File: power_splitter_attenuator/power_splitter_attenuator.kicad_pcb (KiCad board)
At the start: 4 copper layers, 46.2 x 46.2 mm, 40 parts, among them J1 SMA, J2 SMA, J3 SMA, J4 SMA, J5 SMA, J6 SMA, J7 SMA, J8 SMA

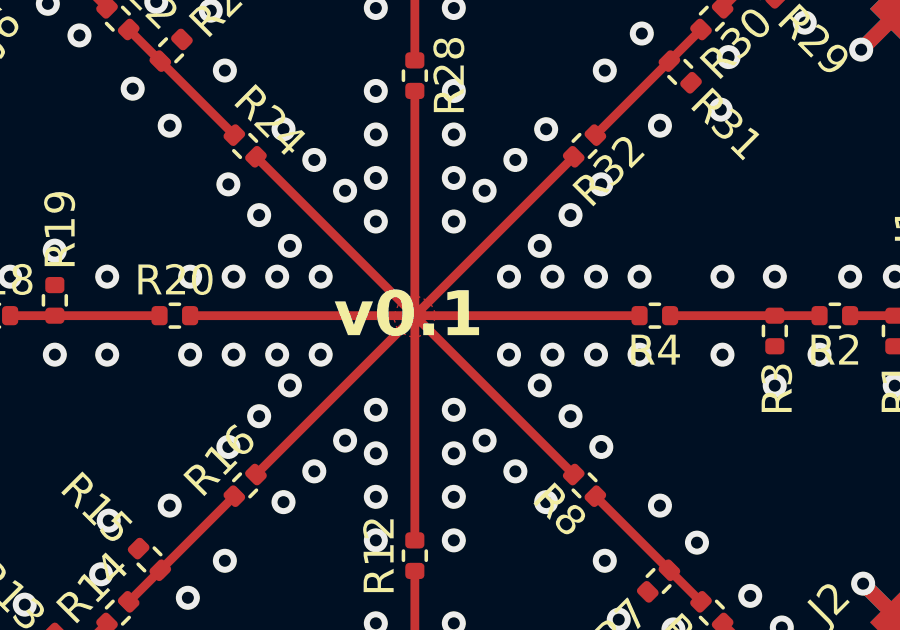
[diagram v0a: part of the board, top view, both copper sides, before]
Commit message: power splitter: update version number to 0.1.1
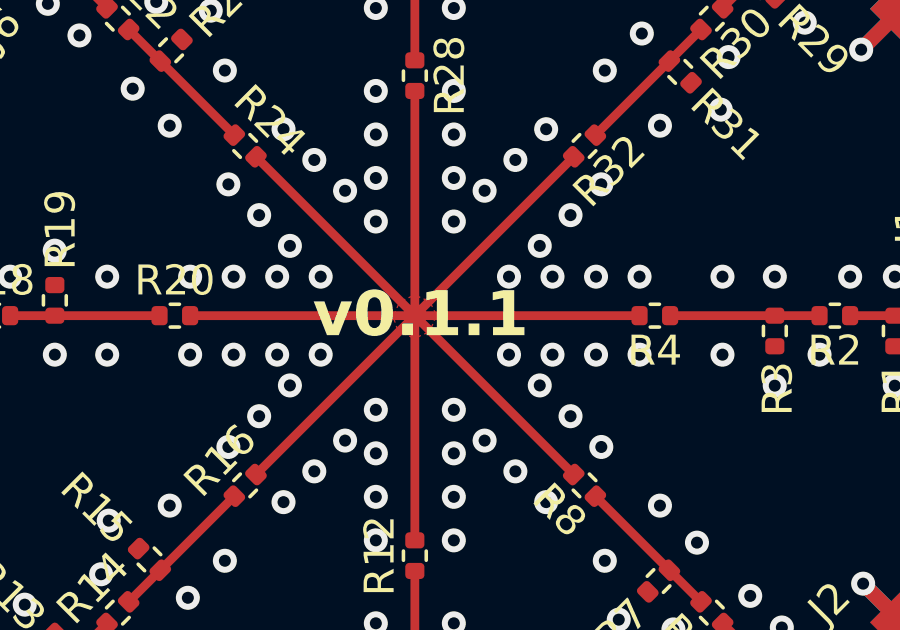
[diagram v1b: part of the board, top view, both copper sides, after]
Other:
- board text added: "v0.1.1"
- board text removed: "v0.1"
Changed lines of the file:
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@@
       (drillshape 0)
       (scaleselection 1)
-      (outputdirectory "output/v0.1.0/gerber/")
+      (outputdirectory "output/v0.1.1/gerber/")
     )
   )
@@
   (gr_circle (center 151.122048 100.092436) (end 152.422048 100.092436)
     (stroke (width 0.1) (type default)) (fill none) (layer "Edge.Cuts"))
-  (gr_text "v0.1" (at 140 80.6) (layer "F.SilkS")
+  (gr_text "v0.1.1" (at 139.3 80.6) (layer "F.SilkS")
     (effects (font (size 1.5 1.5) (thickness 0.3) bold) (justify left bottom))
   )

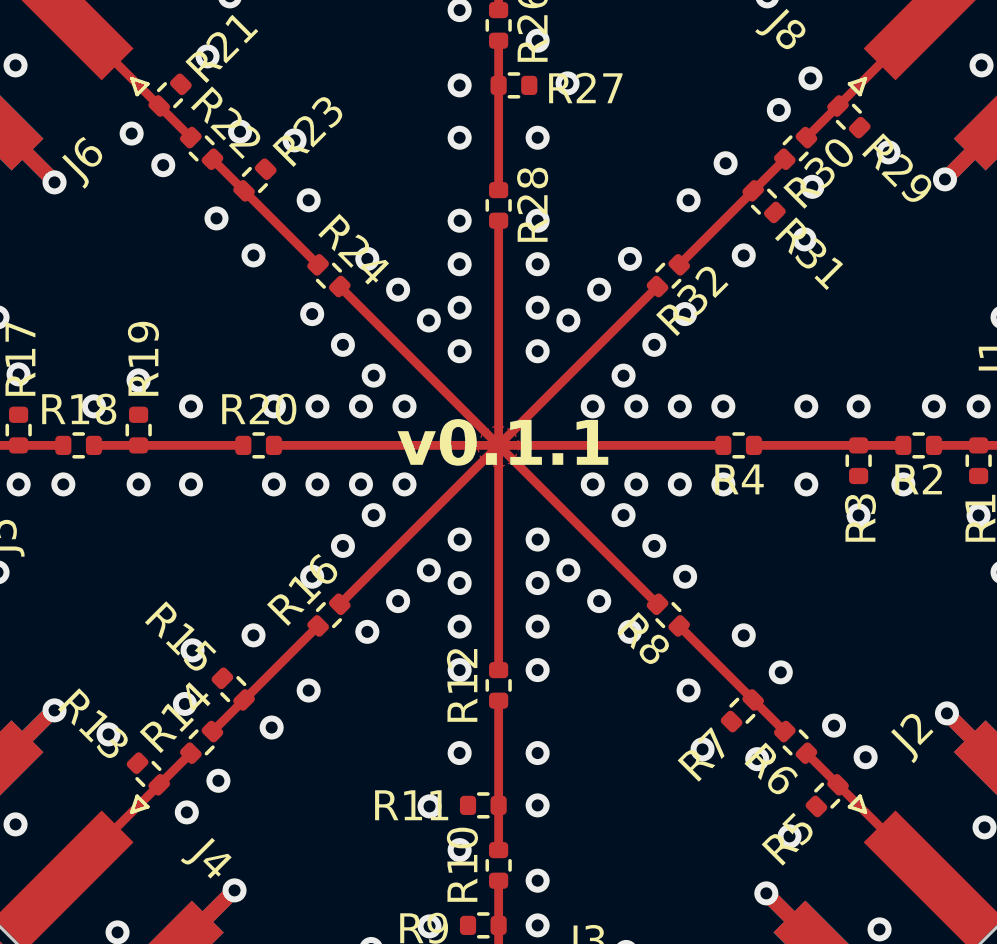
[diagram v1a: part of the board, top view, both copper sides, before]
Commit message: power splitter attenuator: update files to KiCad 9
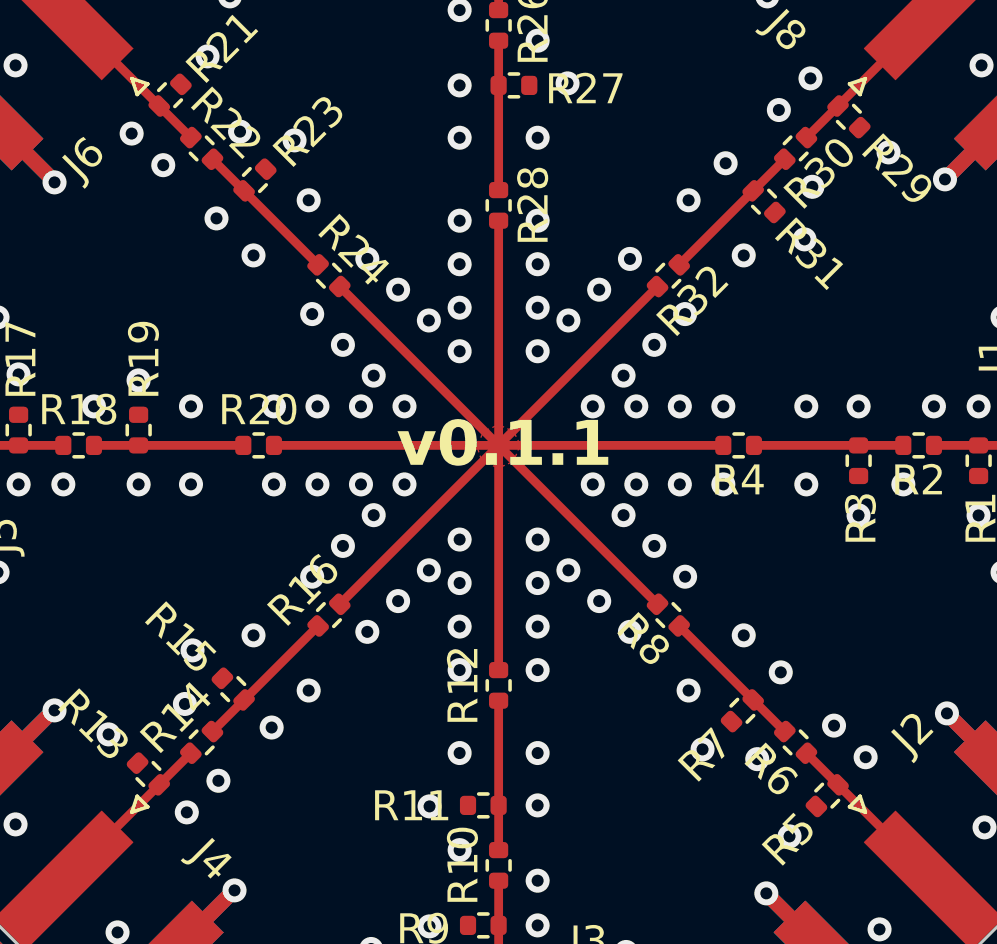
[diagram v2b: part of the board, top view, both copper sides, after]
